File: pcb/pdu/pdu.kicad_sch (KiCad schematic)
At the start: 46 parts, among them J1 CONN_PCIE_PWR_8PIN, J2 MOLEX_0039291087, J3 MOLEX_0039291048, J4 MOLEX_0039291048, J5 CONN_IBC_MGMT_DEVICE, J6 CONN_IBC_MGMT_HOST, M1 LOGO, M2 LOGO, M3 LOGO, M4 LOGO, U1 INA230, U2 AT30TS74_UDFN, U3 TCA6424A, U4 NCP45560IMNTWG-H, U5 NCP45560IMNTWG-H, U6 INA230, U7 NCP45560IMNTWG-H, U8 INA230

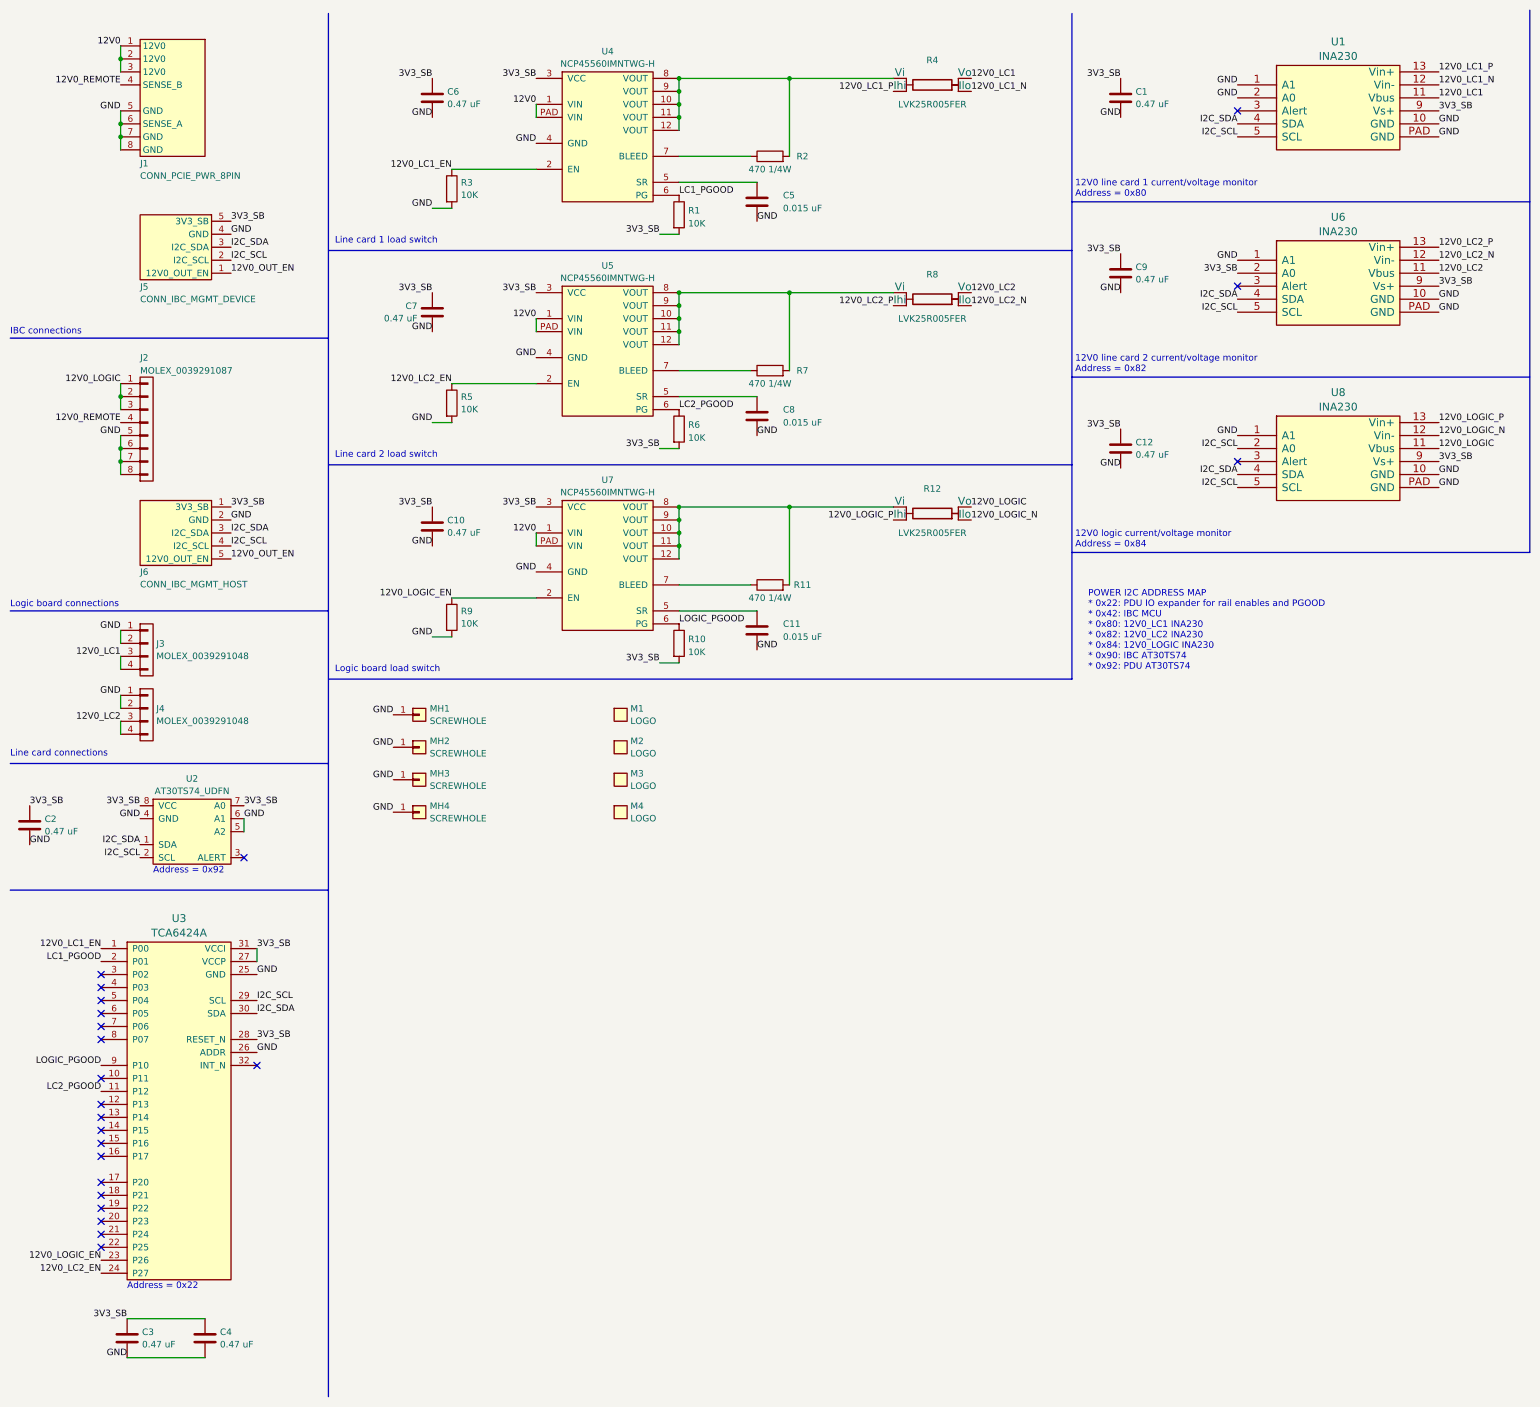
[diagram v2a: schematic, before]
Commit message: PDU: fixed incorrect I2C address note in schematic
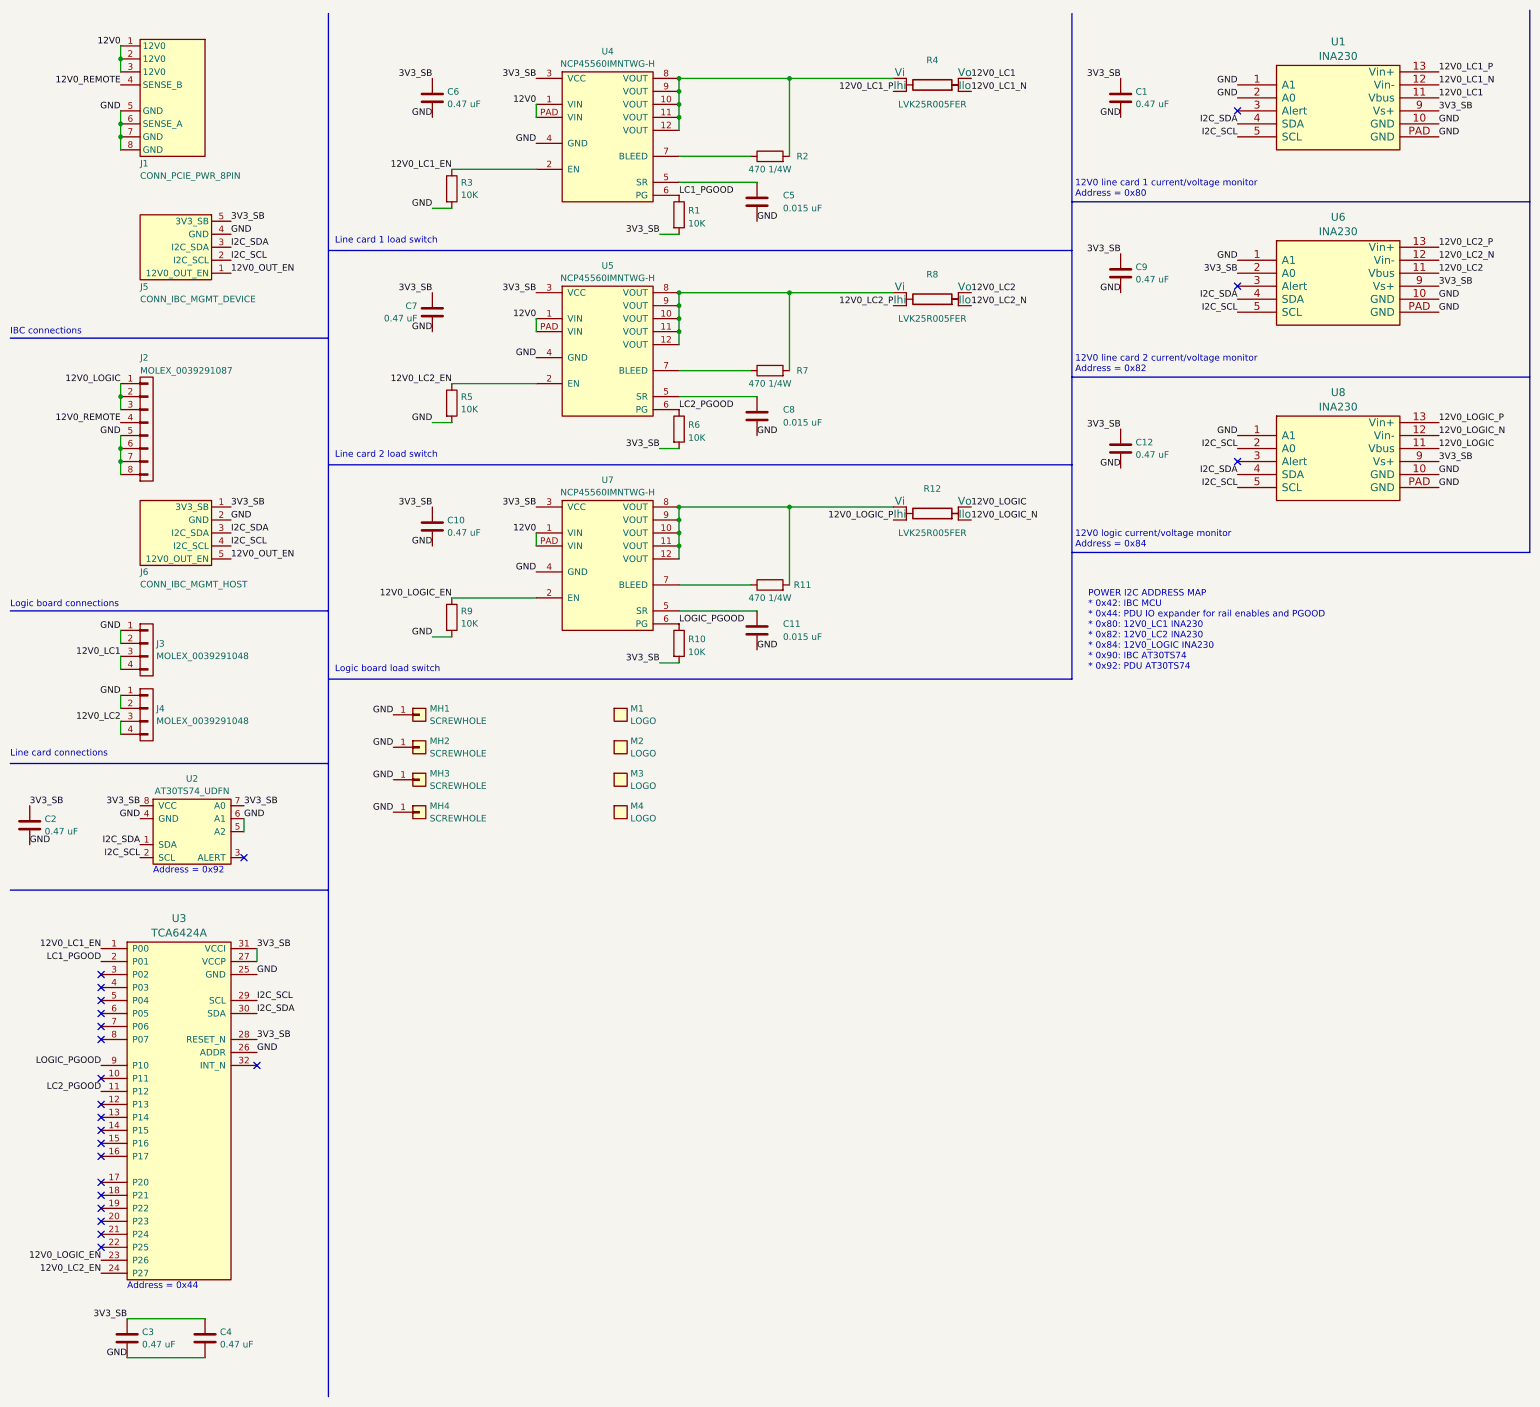
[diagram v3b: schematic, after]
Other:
- note added: "Address = 0x44"
- note added: "POWER I2C ADDRESS MAP * 0x42: IBC MCU * 0x44: PDU IO expander for rail enables and PGOOD * 0x80: 12V0_LC1 INA230 * 0x82: 12V0_LC2 INA230 * 0x84: 12V0_LOGIC INA230 * 0x90: IBC AT30TS74 * 0x92: PDU AT30TS74"
- note removed: "Address = 0x22"
- note removed: "POWER I2C ADDRESS MAP * 0x22: PDU IO expander for rail enables and PGOOD * 0x42: IBC MCU * 0x80: 12V0_LC1 INA230 * 0x82: 12V0_LC2 INA230 * 0x84: 12V0_LOGIC INA230 * 0x90: IBC AT30TS74 * 0x92: PDU AT30TS74"
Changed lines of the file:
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@@
 		)
 	)
-	(text "Address = 0x22"
+	(text "Address = 0x44"
 		(exclude_from_sim no)
 		(at 35.56 261.62 0)
@@
 		)
 	)
-	(text "POWER I2C ADDRESS MAP\n* 0x22: PDU IO expander for rail enables and PGOOD\n* 0x42: IBC MCU\n* 0x80: 12V0_LC1 INA230\n* 0x82: 12V0_LC2 INA230\n* 0x84: 12V0_LOGIC INA230\n* 0x90: IBC AT30TS74\n* 0x92: PDU AT30TS74"
+	(text "POWER I2C ADDRESS MAP\n* 0x42: IBC MCU\n* 0x44: PDU IO expander for rail enables and PGOOD\n* 0x80: 12V0_LC1 INA230\n* 0x82: 12V0_LC2 INA230\n* 0x84: 12V0_LOGIC INA230\n* 0x90: IBC AT30TS74\n* 0x92: PDU AT30TS74"
 		(exclude_from_sim no)
 		(at 223.52 133.35 0)
